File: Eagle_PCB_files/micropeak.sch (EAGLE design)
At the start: 15 parts, among them U1 ATTINY85-20MUR, U2 MS5611-01BA03

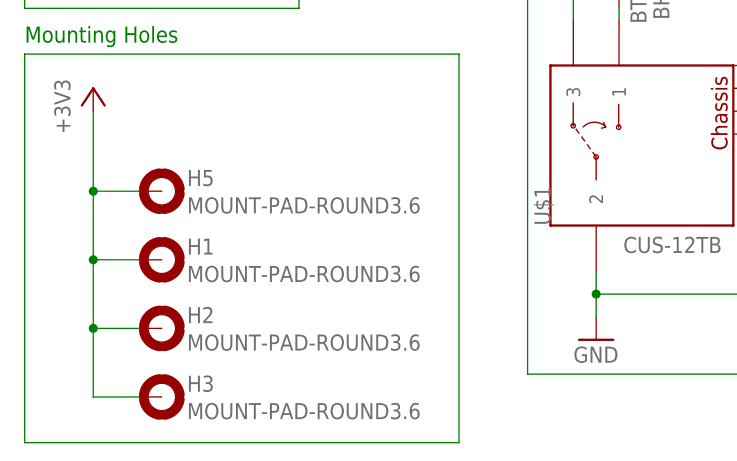
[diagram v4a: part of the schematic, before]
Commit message: replaced mounting holes with correct size hole
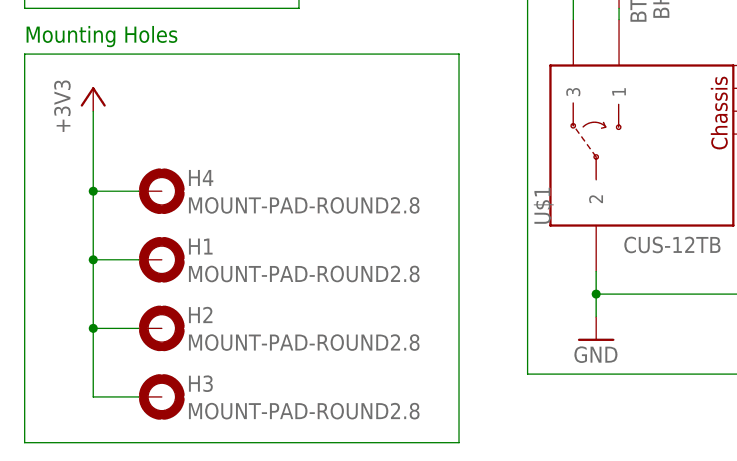
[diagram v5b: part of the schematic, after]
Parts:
- removed H5: MOUNT-PAD-ROUND3.6, holes:MOUNT-PAD-ROUND3.6
- added H4: MOUNT-PAD-ROUND2.8, holes:MOUNT-PAD-ROUND2.8
- H1, H2, H3: value MOUNT-PAD-ROUND3.6 -> MOUNT-PAD-ROUND2.8; device holes:MOUNT-PAD-ROUND3.6 -> holes:MOUNT-PAD-ROUND2.8
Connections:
- net +3V3: now also H4.MOUNT; no longer H5.MOUNT
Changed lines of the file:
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@@
 <part name="GND5" library="supply1" library_urn="urn:adsk.eagle:library:371" deviceset="GND" device=""/>
 <part name="+3V4" library="supply1" library_urn="urn:adsk.eagle:library:371" deviceset="+3V3" device=""/>
-<part name="H5" library="holes" library_urn="urn:adsk.eagle:library:237" deviceset="MOUNT-PAD-ROUND" device="3.6" package3d_urn="urn:adsk.eagle:package:14284/1"/>
-<part name="H1" library="holes" library_urn="urn:adsk.eagle:library:237" deviceset="MOUNT-PAD-ROUND" device="3.6" package3d_urn="urn:adsk.eagle:package:14284/1"/>
-<part name="H2" library="holes" library_urn="urn:adsk.eagle:library:237" deviceset="MOUNT-PAD-ROUND" device="3.6" package3d_urn="urn:adsk.eagle:package:14284/1"/>
-<part name="H3" library="holes" library_urn="urn:adsk.eagle:library:237" deviceset="MOUNT-PAD-ROUND" device="3.6" package3d_urn="urn:adsk.eagle:package:14284/1"/>
 <part name="+3V5" library="supply1" library_urn="urn:adsk.eagle:library:371" deviceset="+3V3" device=""/>
 <part name="LED1" library="led" library_urn="urn:adsk.eagle:library:259" deviceset="LED" device="P-LCC-2" package3d_urn="urn:adsk.eagle:package:15817/1"/>
+<part name="H4" library="holes" library_urn="urn:adsk.eagle:library:237" deviceset="MOUNT-PAD-ROUND" device="2.8" package3d_urn="urn:adsk.eagle:package:14281/1"/>
+<part name="H1" library="holes" library_urn="urn:adsk.eagle:library:237" deviceset="MOUNT-PAD-ROUND" device="2.8" package3d_urn="urn:adsk.eagle:package:14281/1"/>
+<part name="H2" library="holes" library_urn="urn:adsk.eagle:library:237" deviceset="MOUNT-PAD-ROUND" device="2.8" package3d_urn="urn:adsk.eagle:package:14281/1"/>
+<part name="H3" library="holes" library_urn="urn:adsk.eagle:library:237" deviceset="MOUNT-PAD-ROUND" device="2.8" package3d_urn="urn:adsk.eagle:package:14281/1"/>
 </parts>
 <sheets>
@@
 <attribute name="VALUE" x="35.56" y="90.17" size="1.778" layer="96" rot="R90"/>
 </instance>
-<instance part="H5" gate="G$1" x="48.26" y="45.72" smashed="yes">
+<instance part="+3V5" gate="G$1" x="40.64" y="57.15" smashed="yes">
+<attribute name="VALUE" x="38.1" y="52.07" size="1.778" layer="96" rot="R90"/>
+</instance>
+<instance part="LED1" gate="G$1" x="194.056" y="135.89" smashed="yes" rot="R90">
+<attribute name="NAME" x="198.628" y="139.446" size="1.778" layer="95" rot="R180"/>
+<attribute name="VALUE" x="198.628" y="141.605" size="1.778" layer="96" rot="R180"/>
+</instance>
+<instance part="H4" gate="G$1" x="48.26" y="45.72" smashed="yes">
 <attribute name="NAME" x="51.054" y="46.3042" size="1.778" layer="95"/>
 <attribute name="VALUE" x="51.054" y="43.2562" size="1.778" layer="96"/>
@@
 <attribute name="NAME" x="51.054" y="23.4442" size="1.778" layer="95"/>
 <attribute name="VALUE" x="51.054" y="20.3962" size="1.778" layer="96"/>
-</instance>
-<instance part="+3V5" gate="G$1" x="40.64" y="57.15" smashed="yes">
-<attribute name="VALUE" x="38.1" y="52.07" size="1.778" layer="96" rot="R90"/>
-</instance>
-<instance part="LED1" gate="G$1" x="194.056" y="135.89" smashed="yes" rot="R90">
-<attribute name="NAME" x="198.628" y="139.446" size="1.778" layer="95" rot="R180"/>
-<attribute name="VALUE" x="198.628" y="141.605" size="1.778" layer="96" rot="R180"/>
 </instance>
 </instances>
@@
 </segment>
 <segment>
-<pinref part="H5" gate="G$1" pin="MOUNT"/>
 <wire x1="45.72" y1="45.72" x2="40.64" y2="45.72" width="0.1524" layer="91"/>
 <wire x1="40.64" y1="45.72" x2="40.64" y2="54.61" width="0.1524" layer="91"/>
 <pinref part="+3V5" gate="G$1" pin="+3V3"/>
-<pinref part="H1" gate="G$1" pin="MOUNT"/>
 <wire x1="45.72" y1="38.1" x2="40.64" y2="38.1" width="0.1524" layer="91"/>
 <wire x1="40.64" y1="38.1" x2="40.64" y2="45.72" width="0.1524" layer="91"/>
 <junction x="40.64" y="45.72"/>
-<pinref part="H2" gate="G$1" pin="MOUNT"/>
 <wire x1="45.72" y1="30.48" x2="40.64" y2="30.48" width="0.1524" layer="91"/>
 <wire x1="40.64" y1="30.48" x2="40.64" y2="38.1" width="0.1524" layer="91"/>
 <junction x="40.64" y="38.1"/>
-<pinref part="H3" gate="G$1" pin="MOUNT"/>
 <wire x1="45.72" y1="22.86" x2="40.64" y2="22.86" width="0.1524" layer="91"/>
 <wire x1="40.64" y1="22.86" x2="40.64" y2="30.48" width="0.1524" layer="91"/>
 <junction x="40.64" y="30.48"/>
-</segment>
-</net>
+<pinref part="H4" gate="G$1" pin="MOUNT"/>
+<pinref part="H1" gate="G$1" pin="MOUNT"/>
+<pinref part="H2" gate="G$1" pin="MOUNT"/>
+<pinref part="H3" gate="G$1" pin="MOUNT"/>
+</segment>
+</net>
